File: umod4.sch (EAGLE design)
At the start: 74 parts, among them IC3 27C256-FEED-THRU, J1 DM3AT-SF-PEJ, J2 10118194-0001LF, J3 CON-1X8-VERT, M1 RPi Pico W, M2 Generic single-sided NEO-8, Q1 C10487/SI2301CDS, Q2 SS8050, U1 74LVC541, U2 74LVC4245, U3 74LVC541, U4 RP2040, U5 W25Q128JVSIQ, U6 74LVC2G04, U7 74LVC2G04, Y1 12MHz

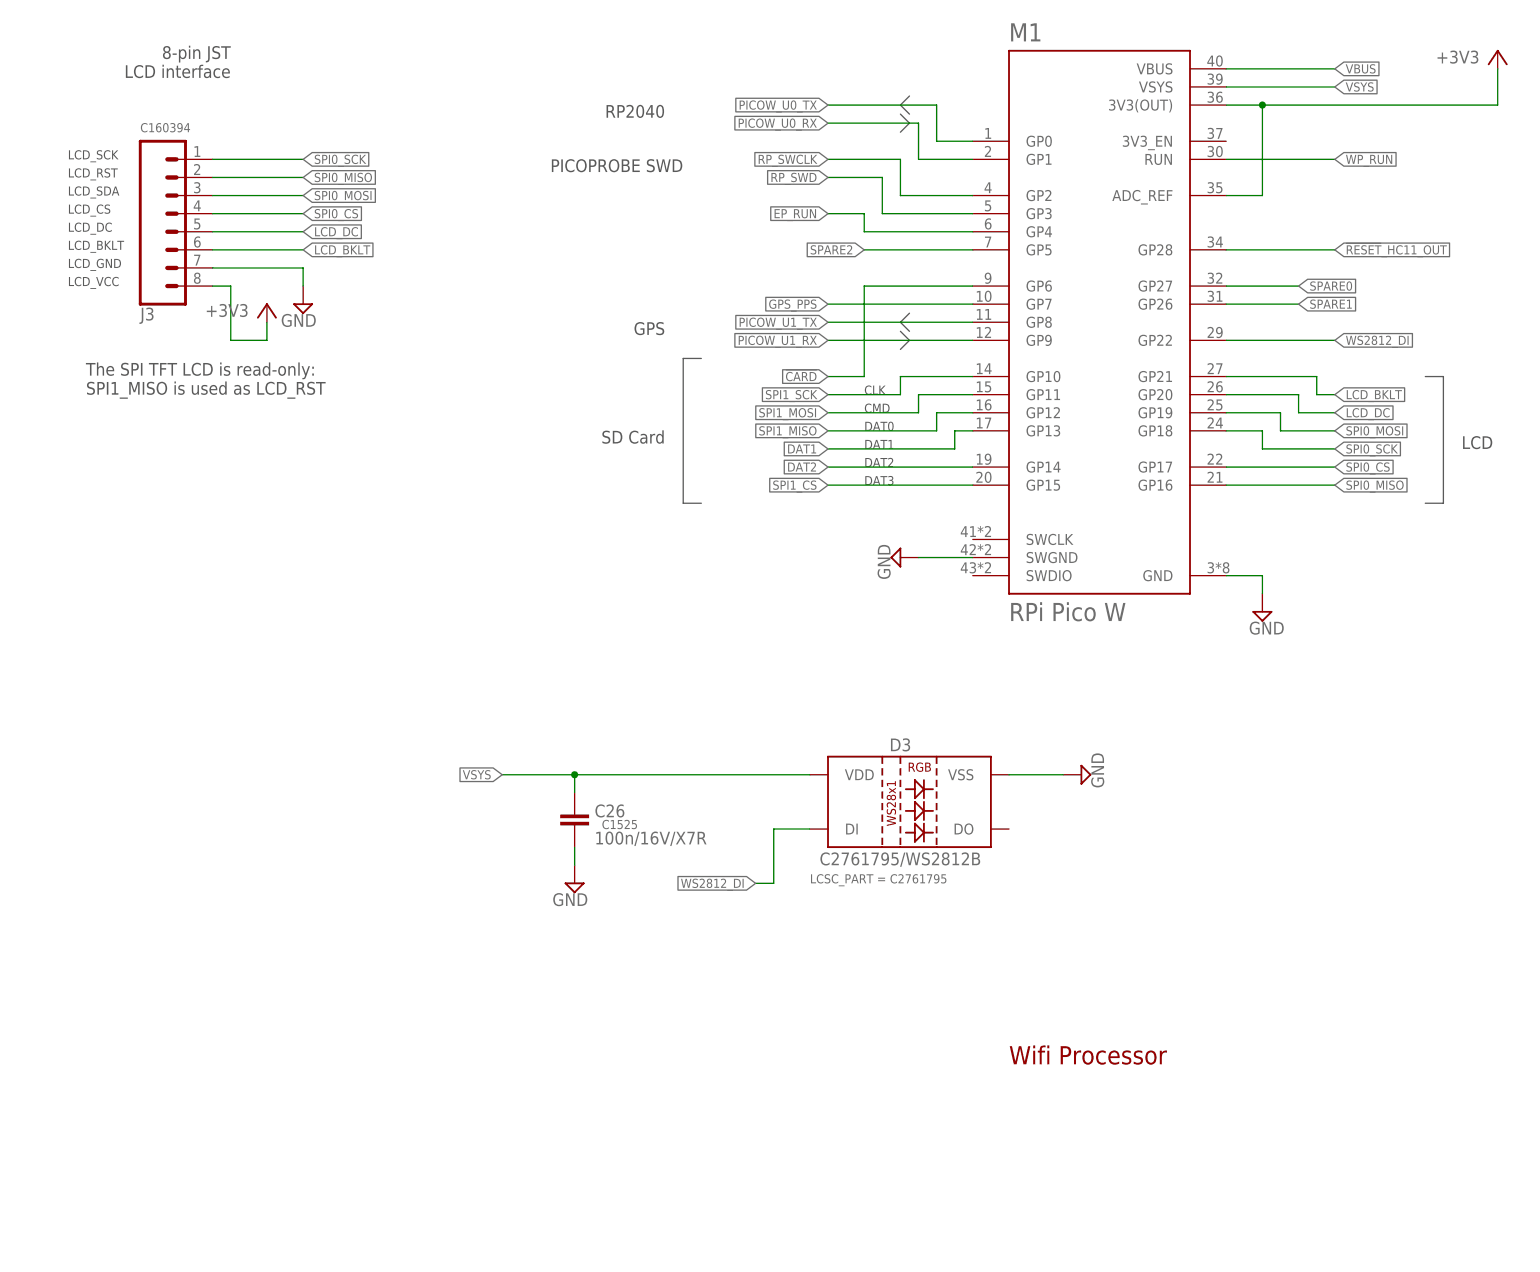
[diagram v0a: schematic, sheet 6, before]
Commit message: Updates for 4V2 work-in-progress
- Latest version of 4V2 incorporating changes as per Changelist-4V2.md
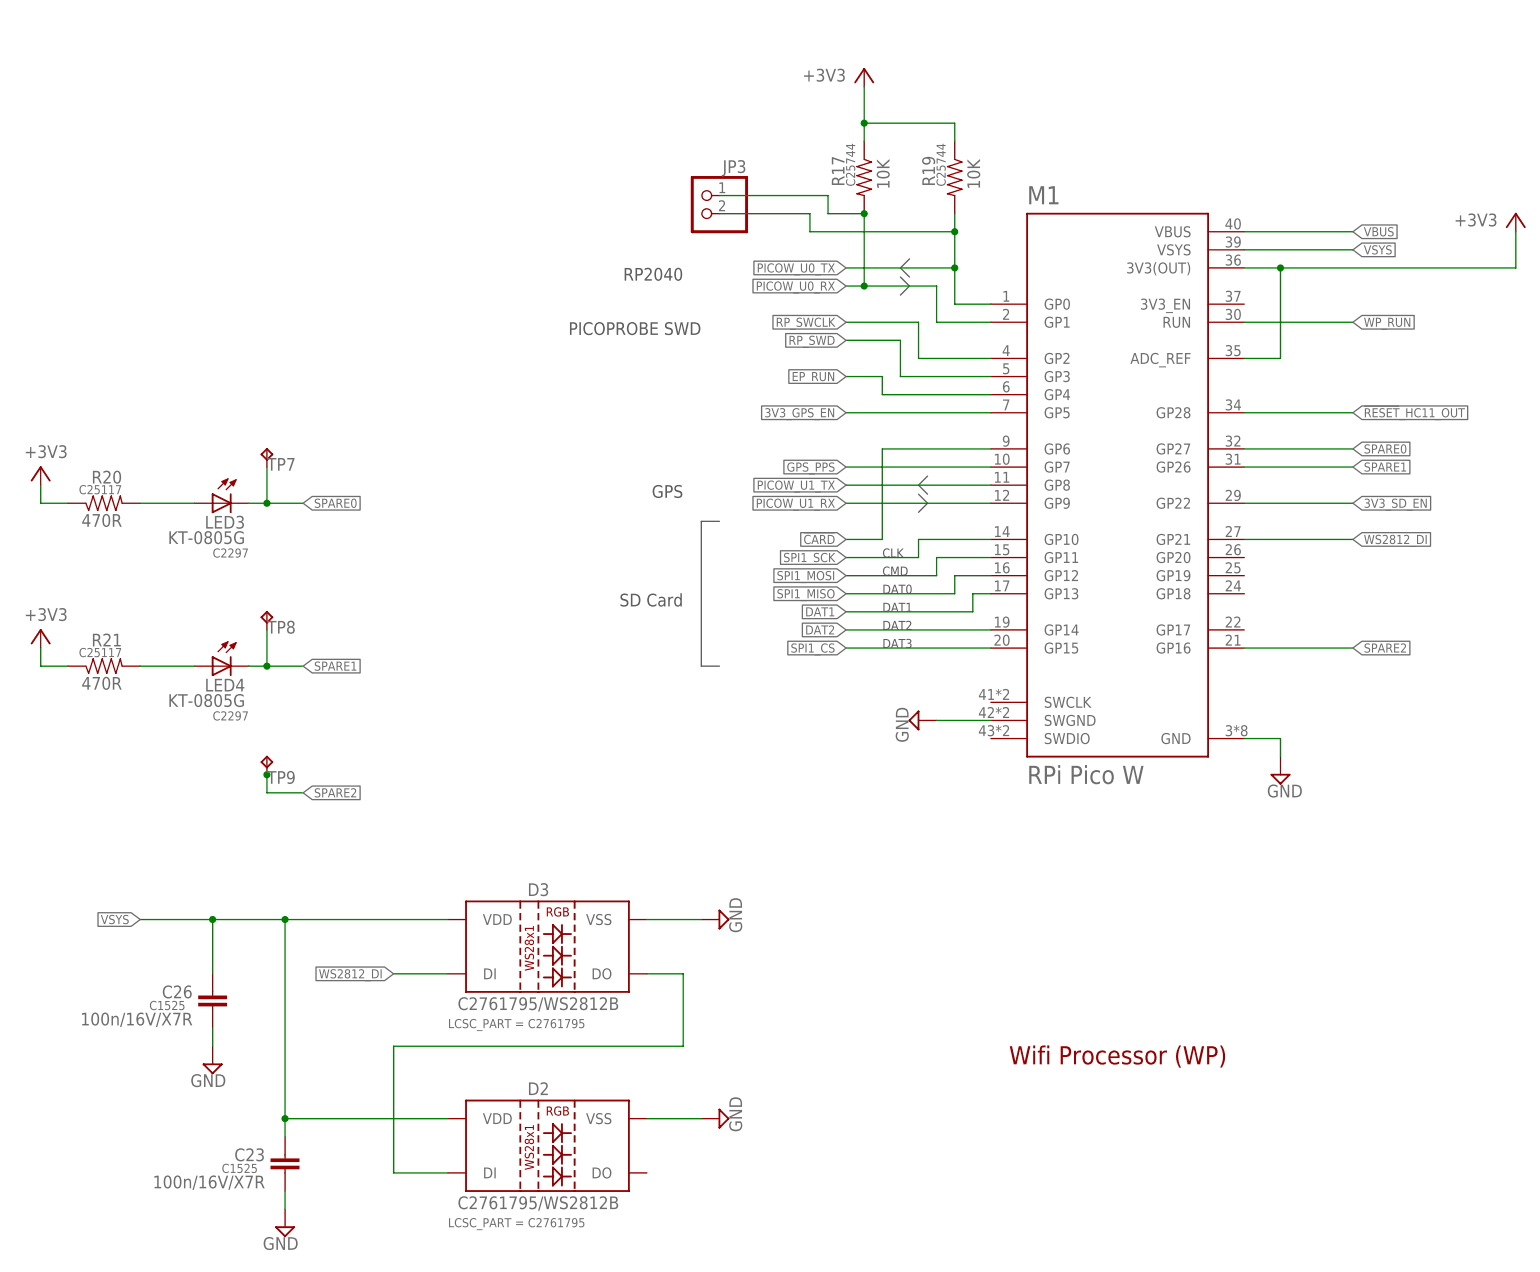
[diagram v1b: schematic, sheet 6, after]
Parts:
- removed C25: 100n/16V/X7R, SparkFun-03-01-2010:CAP0402-CAP
- removed J3: CON-1X8-VERT, robins-v7:CON-1X8-VERT
- removed U7: 74LVC2G04, robins-v7:74LVC2G04-SOT23-6
- added 1V1: TPB1,27, testpad:TPB1,27
- added C13, C28: 1u/25V/X5R, SparkFun-03-01-2010:CAP0402-CAP
- added D2, D4: C2761795/WS2812B, SparkFun-LED:WS2812B
- added JP5, JP6: JUMPER-SMT_3_1-NC_TRACE_NO-SILK, SparkFun-Jumpers:JUMPER-SMT_3_1-NC_TRACE_NO-SILK
- added LED3, LED4: KT-0805G, led:LEDSML0805
- added Q3, Q4: C10487/SI2301CDS, robins-v7:FET-P-CHANNELSI2369DS
- added R17, R19, R22, R24: 10K, SparkFun-03-01-2010:RESISTOR0402-RES
- added R20, R21: 470R, SparkFun-03-01-2010:RESISTOR0402-RES
- added R23, R25: 1K, SparkFun-03-01-2010:RESISTOR0402-RES
- added TP7, TP8, TP9: (no value), robins-v7:TEST-POINT-1035
- added U8: 3.3V/150mA, SparkFun-IC-Power:V_REG_MIC52053.3V
- JP3: value NC -> (none); device SparkFun-Jumpers:JUMPER-SMT_2_NC_TRACE_NO-SILK -> pinhead:PINHD-1X2
- R1: value 10K -> 1K; LCSC_PART C25744 -> C11702
- R2: value 5K1 -> 100R; LCSC_PART C25905 -> (none)
- R9: value 2.2K -> 100R; LCSC_PART C25879 -> (none)
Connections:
- removed net !ECU_PWR!: U1.!OE1, U3.!OE1, U6G$2.O
- removed net LCD_BKLT: J3.6, M1.GP21
- removed net LCD_DC: J3.5, M1.GP20
- removed net NC1_IN: JP3.2, U7G$2.I
- removed net NC1_OUT: U7G$2.O
- removed net SPI0_CS: J3.4, M1.GP17
- removed net SPI0_MISO: J3.2, M1.GP16
- removed net SPI0_MOSI: J3.3, M1.GP19
- removed net SPI0_SCK: J3.1, M1.GP18
- new net 3V3_GPS_EN: M1.GP5, R22.1, R23.2
- new net 3V3_SD_EN: M1.GP22, R24.2, R25.1
- new net 3V3_SD_SW: JP5.3, Q4.S
- new net 3V3_SW: JP6.3, Q3.S
- new net N$16: R9.1, U4.SWD
- new net N$19: D2.DI, D3.DO
- new net N$21: LED3.A, R20.2
- new net N$22: LED4.A, R21.2
- new net N$23: Q4.G, R25.2
- new net N$25: Q3.G, R23.1
- new net VCCB: C1.1, C13.1, C2.1, C3.1, C4.1, C6.1, R1.1, U1.VCC, U2.VCCB@1, U2.VCCB@2, U3.VCC, U6G$3.VCC, U8.OUT
- new net VCC_GPS: JP6.2, M2.VCC, R8.2
- new net VDD_SD: C14.1, C27.1, J1.VDD, JP5.2, R15.2, R16.2
- net !CE!_5V: now also U6G$2.I; no longer U7G$1.I
- net +3V3: now also JP5.1, JP6.1, Q3.D, Q4.D, R17.1, R19.1, R20.1, R21.1, R22.2; no longer C1.1, C14.1, C2.1, C23.1, C25.1, C27.1, C3.1, C4.1, C6.1, J1.VDD, J3.8, M2.VCC, R15.2, R16.2, R8.2, U1.VCC, U2.VCCB@1, U2.VCCB@2, U3.VCC, U6G$3.VCC, U7G$3.VCC
- net +5_ECU: now also C28.1, U8.EN, U8.IN; no longer R2.1, R9.1
- net 1.0V: now also 1V1.TP
- net CE: now also U6G$2.O; no longer U7G$1.O
- net DBG_BSY: now also D4.DI
- net GND: now also C13.2, C28.2, D2.VSS, D4.VSS, R24.1, U1.!OE1, U3.!OE1, U8.GND; no longer C25.2, J3.7, JP3.1, R1.2, U7G$3.GND
- net N$3: now also R1.2; no longer R9.2
- net N$4: now also R2.1, U4.SWCLK; no longer C24.1, R1.1, R2.2, U6G$2.I
- net PICOW_U0_RX: now also JP3.1, R17.2
- net PICOW_U0_TX: now also JP3.2, R19.2
- net RP_SWCLK: now also R2.2; no longer U4.SWCLK
- net RP_SWD: now also R9.2; no longer U4.SWD
- net SPARE0: now also LED3.C, TP7.TP
- net SPARE1: now also LED4.C, TP8.TP
- net SPARE2: now also M1.GP16, TP9.TP; no longer M1.GP5
- net VSYS: now also C23.1, C24.1, D2.VDD, D4.VDD
- net WS2812_DI: now also M1.GP21; no longer M1.GP22
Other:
- note added: "Approx 1.1 mA assuming Vf of 2.2V"
- note added: "Default is to power SD Card via 3V3_SD_SW. If desired, cut the jumper and solder the other side to power SD card permanently via +3V3."
- note added: "Default: DISABLED '1': ENABLED"
- note added: "Default: ENABLED '0': DISABLED"
- note added: "Eprom Emulator Processor (EP)"
- note added: "LED2 lights only when ECU is powered."
- note added: "Wifi Processor (WP)"
- note removed: "!CE! does not need to be complemented but we do need the voltage translation that the inverter provides"
- note removed: "8-pin JST LCD interface"
- note removed: "A V divider is not required, but noise filtering might be useful. Also, R1 is required if a bare umod4 is powered on a bench, no ECU."
- note removed: "Approx 1.2 mA assuming Vf of 2.2V"
- note removed: "Eprom Emulator"
- note removed: "LCD"
- note removed: "LCD_BKLT"
- note removed: "LCD_CS"
- note removed: "LCD_DC"
- note removed: "LCD_GND"
- note removed: "LCD_RST"
- note removed: "LCD_SCK"
- note removed: "LCD_SDA"
- note removed: "LCD_VCC"
- note removed: "The SPI TFT LCD is read-only: SPI1_MISO is used as LCD_RST"
- note removed: "Wifi Processor"
- moved on the sheet: C10, C11, C12, C14, C16, C22, C26, C27, C5, C6, C7, C9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
